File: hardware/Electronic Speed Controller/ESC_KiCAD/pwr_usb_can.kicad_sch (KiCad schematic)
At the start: 31 parts, among them J1 XT60, J3 2x2-2.54MM, J4 S2B-PH-K-S, J5 S2B-PH-K-S, J6 USB TYPE-A, U1 R-78CK5.0-0.5, U2 TLV75533PDBVR, U6 SN65HVD232DR, U8 LM66200DRLR

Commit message: change drivers to C++, add software IIR filtering, improve GCS software
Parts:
- J3: value 2x2-2.54MM -> 2x2-2.54MM
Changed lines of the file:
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@@
 			)
 		)
-		(property "Value" "2x2-2.54MM "
+		(property "Value" "2x2-2.54MM"
 			(at 116.586 135.89 90)
 			(effects

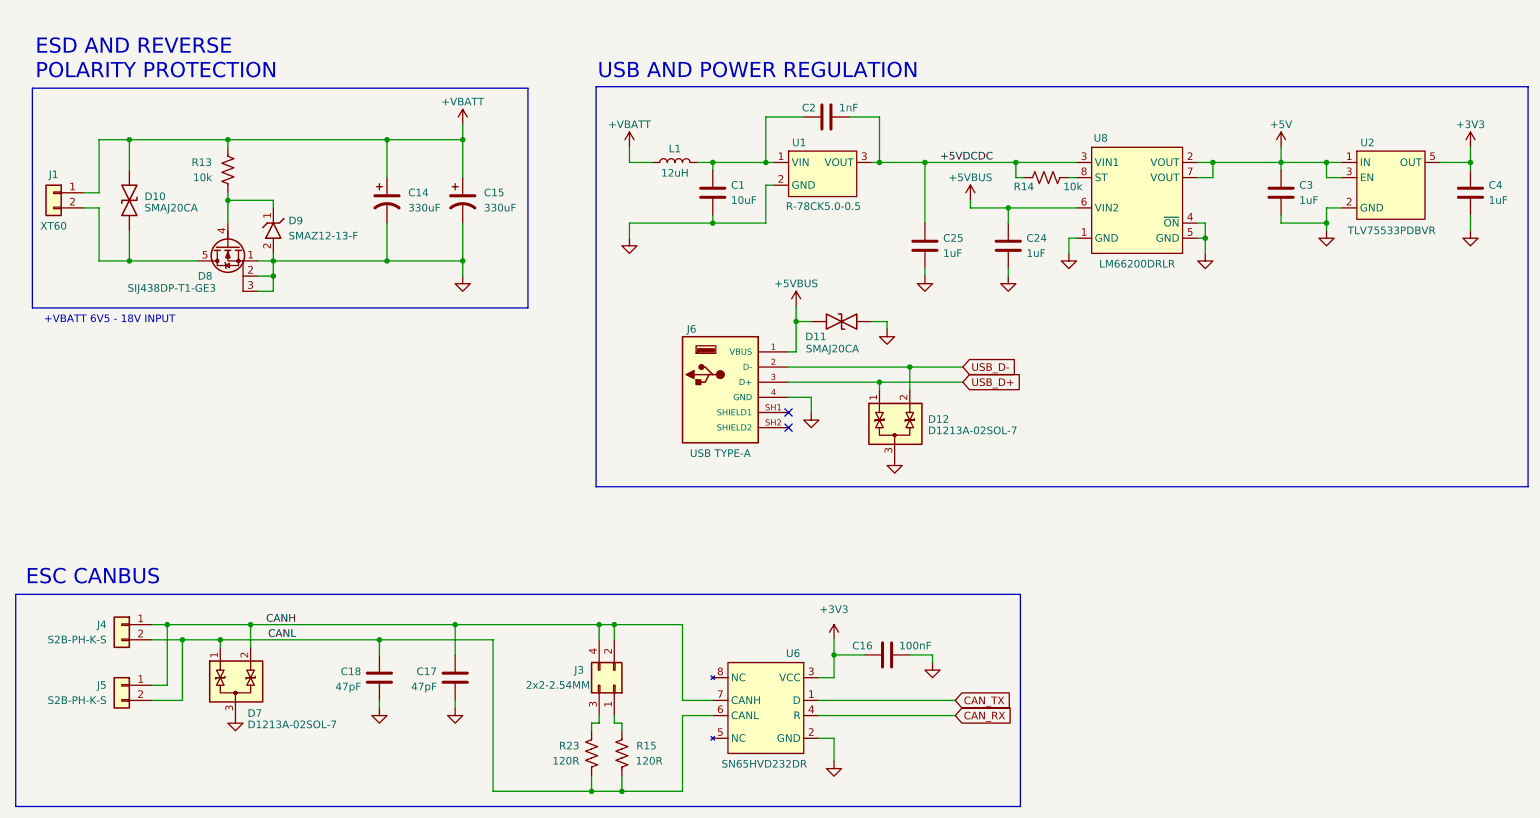
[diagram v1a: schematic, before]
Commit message: finish ESC hardware RevA, CC2500 driver working
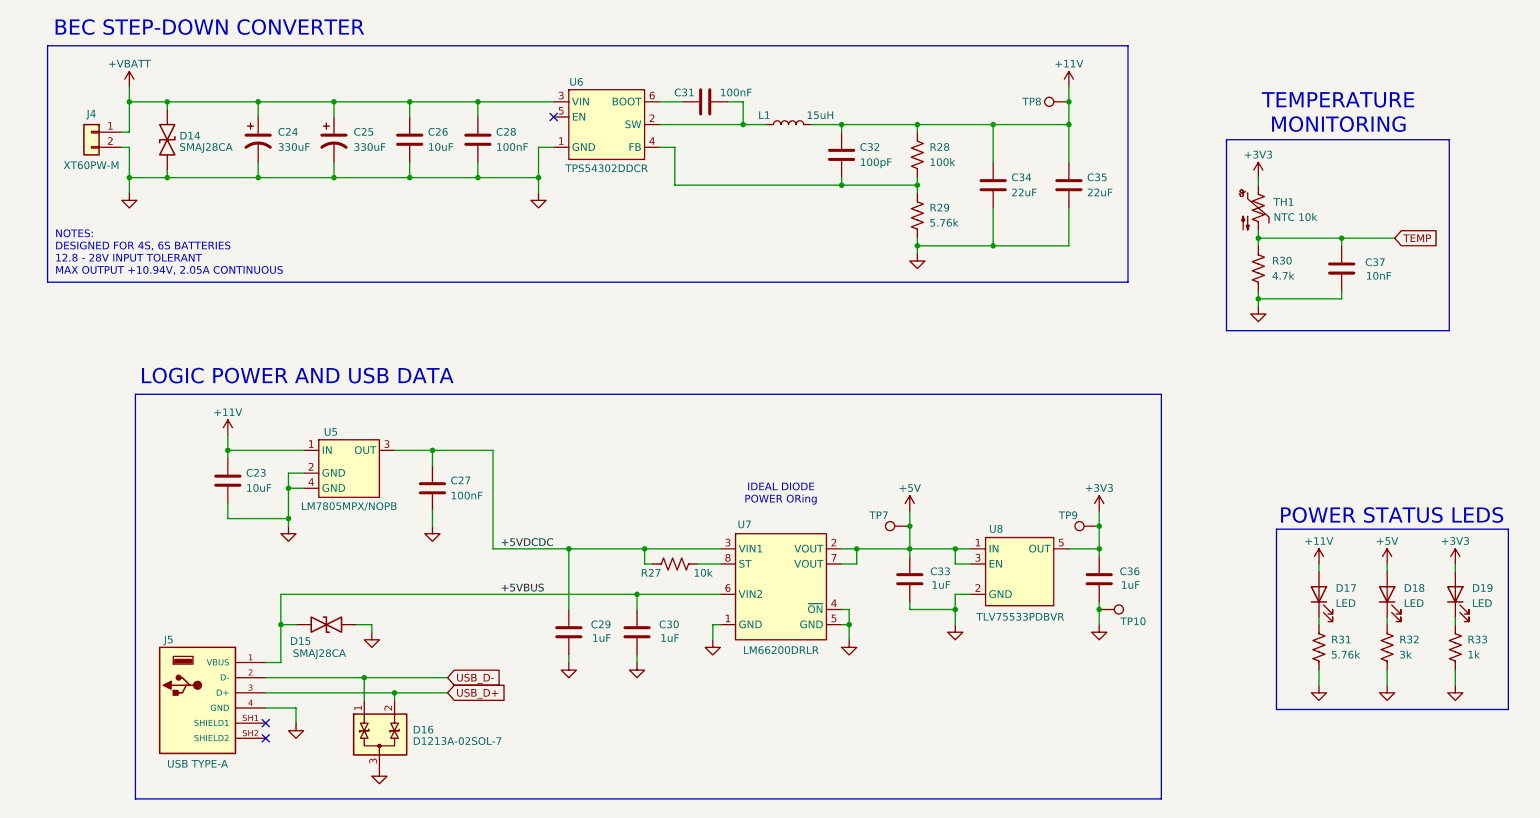
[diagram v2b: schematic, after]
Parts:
- removed C1: 10uF, Capacitors:CAP_1206_3216Metric, symbol Device:C
- removed C14, C15: 330uF, Capacitors:CAP_ALUM_HORIZONTAL, symbol Device:C_Polarized_US
- removed C16: 100nF, Capacitors:CAP_0603_1608Metric, symbol Device:C
- removed C17, C18: 47pF, Capacitors:CAP_0603_1608Metric, symbol Device:C
- removed C2: 1nF, Capacitors:CAP_0603_1608Metric, symbol Device:C
- removed C24, C25, C3, C4: 1uF, Capacitors:CAP_0603_1608Metric, symbol Device:C
- removed D10, D11: SMAJ20CA, Diodes:Littelfuse_SMA, symbol Diodes:TVS_BIDIRECTIONAL
- removed D12, D7: D1213A-02SOL-7, Diodes:DiodesINC_SOT23-3, symbol Diodes:TVS_BIDIRECTIONAL_2CH
- removed D8: SIJ438DP-T1-GE3, Diodes:Vishay_PPAK_SO-8L, symbol Diodes:SiJ438DP
- removed D9: SMAZ12-13-F, Diodes:DiodesINC_SMA, symbol Diodes:ZENER
- removed J1: XT60, Connectors:CONN_MALE_TH_XT60, symbol Connector_Generic:Conn_01x02
- removed J3: 2x2-2.54MM, Connectors:CONN_MALE_TH_2.54MM_2x2, symbol Connector_Generic:Conn_02x02_Odd_Even
- removed J5: S2B-PH-K-S, Connectors:CONN_JST_S2B-PH-K-S, symbol Connector_Generic:Conn_01x02
- removed J6: USB TYPE-A, Connectors:USB2.0_4P_AMPHENOL_87583-2010BLF, symbol Connectors:USB2.0-4P-2SH
- removed R13, R14: 10k, Resistors:RES_0603_1608Metric, symbol Device:R_US
- removed R15, R23: 120R, Resistors:RES_0603_1608Metric, symbol Device:R_US
- removed U1: R-78CK5.0-0.5, ICs:RECOM_SIP-3, symbol ICs:R-78CKxx-0.5
- removed U2: TLV75533PDBVR, ICs:TI_SOT23-5, symbol ICs:TLV755P-DBV
- removed U6: SN65HVD232DR, ICs:TI_SOIC-8, symbol ICs:SN65HVD232D
- removed U8: LM66200DRLR, ICs:TI_SOT-5X3, symbol ICs:LM66200
- added C23, C26: 10uF, Capacitors:CAP_1206_3216Metric, symbol Device:C
- added C24, C25: 330uF, Capacitors:CAP_ALUM_HORIZONTAL, symbol Device:C_Polarized_US
- added C27, C28, C31: 100nF, Capacitors:CAP_0603_1608Metric, symbol Device:C
- added C29, C30, C33, C36: 1uF, Capacitors:CAP_0805_2012Metric, symbol Device:C
- added C32: 100pF, Capacitors:CAP_0603_1608Metric, symbol Device:C
- added C34, C35: 22uF, Capacitors:CAP_0805_2012Metric, symbol Device:C
- added C37: 10nF, Capacitors:CAP_0603_1608Metric, symbol Device:C
- added D14, D15: SMAJ28CA, Diodes:Littelfuse_SMA, symbol Diodes:TVS_BIDIRECTIONAL
- added D16: D1213A-02SOL-7, Diodes:DiodesINC_SOT23-3, symbol Diodes:TVS_BIDIRECTIONAL_2CH
- added D17, D18, D19: LED, Diodes:LED_0603_1608Metric, symbol Device:LED
- added J5: USB TYPE-A, Connectors:USB2.0_4P_AMPHENOL_87583-2010BLF, symbol Connectors:USB2.0-4P-2SH
- added R27: 10k, Resistors:RES_0603_1608Metric, symbol Device:R_US
- added R28: 100k, Resistors:RES_0603_1608Metric, symbol Device:R_US
- added R29, R31: 5.76k, Resistors:RES_0603_1608Metric, symbol Device:R_US
- added R30: 4.7k, Resistors:RES_0603_1608Metric, symbol Device:R_US
- added R32: 3k, Resistors:RES_0603_1608Metric, symbol Device:R_US
- added R33: 1k, Resistors:RES_0603_1608Metric, symbol Device:R_US
- added TH1: NTC 10k, Resistors:RES_0603_1608Metric, symbol Device:Thermistor_NTC_US
- added TP10, TP7, TP8, TP9: TestPoint, TestPoint:TestPoint_Pad_2.0x2.0mm, symbol Connector:TestPoint
- added U5: LM7805MPX/NOPB, ICs:TI_SOT223-4, symbol ICs:LM7805-DCY
- added U6: TPS54302DDCR, ICs:TI_SOT23-6, symbol ICs:TPS54302
- added U7: LM66200DRLR, ICs:TI_SOT-5X3, symbol ICs:LM66200
- added U8: TLV75533PDBVR, ICs:TI_SOT23-5, symbol ICs:TLV755P-DBV
- J4: value S2B-PH-K-S -> XT60PW-M; footprint Connectors:CONN_JST_S2B-PH-K-S -> Connectors:CONN_MALE_TH_XT60PW; JLCPCB Part # C173752 -> C98732; Manufacturer JST Sales America Inc. -> Changzhou Amass Elec; Manufacturer Part # S2B-PH-K-S -> XT60PW-M
- L1: value 12uH -> 15uH; footprint Inductors:Abracon_ASPI-6045S -> Inductors:L_6045S; JLCPCB Part # C187451 -> C83374; Manufacturer Abracon LLC -> Shenzhen Sunlord Electronics Co., Ltd.; Manufacturer Part # ASPI-6045S-120M-T -> SWPA6045S150MT
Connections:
- net CANH is gone; now on net +VBATT: J4.1 (Pin_1)
- net CANL is gone; now on net GND: J4.2 (Pin_2)
- net +3V3: now also C36.2, D19.2 (A), TH1.1, TP9.1, U8.5 (OUT)
- net +5V: now also C33.2, D18.2 (A), TP7.1, U7.2 (VOUT), U7.7 (VOUT), U8.1 (IN), U8.3 (EN)
- net +5VBUS: now also C30.2, D15.1 (K), J5.1 (VBUS), U7.6 (VIN2)
- net +5VDCDC: now also C27.2, C29.2, R27.1, U5.3 (OUT), U7.3 (VIN1)
- net +VBATT: now also C24.1, C25.1, C26.1, C28.2, D14.1 (K), U6.3 (VIN); no longer L1.1
- net GND: now also C23.2, C24.2, C25.2, C26.2, C27.1, C28.1, C29.1, C30.1, C33.1, C34.2, C35.2, C36.1, C37.1, D14.2 (A), D15.2 (A), D16.3 (A), J5.4 (GND), R29.2, R30.2, R31.2, R32.2, R33.2, TP10.1, U5.2 (GND), U5.4 (GND), U6.1 (GND), U7.1 (GND), U7.4 (~{ON}), U7.5 (GND), U8.2 (GND)
- net USB_D+: now also D16.2 (K), J5.3 (D+)
- net USB_D-: now also D16.1 (K), J5.2 (D-)
- net +11V: now reaches L1.2
- net +11V: now also C23.1, C32.1, C34.1, C35.1, D17.2 (A), R28.1, TP8.1, U5.1 (IN)
- new net: C32.2, R28.2, R29.1, U6.4 (FB)
- new net: C31.2, L1.1, U6.2 (SW)
- new net: C31.1, U6.6 (BOOT)
- new net: R27.2, U7.8 (ST)
- new net: D19.1 (K), R33.1
- new net: D17.1 (K), R31.1
- new net: D18.1 (K), R32.1
- new net TEMP: C37.2, R30.1, TH1.2
- no-connect marks 2 -> 3
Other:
- note added: "BEC STEP-DOWN CONVERTER"
- note added: "IDEAL DIODE POWER ORing"
- note added: "LOGIC POWER AND USB DATA"
- note added: "NOTES: DESIGNED FOR 4S, 6S BATTERIES 12.8 - 28V INPUT TOLERANT MAX OUTPUT +10.94V, 2.05A CONTINUOUS"
- note added: "POWER STATUS LEDS"
- note added: "TEMPERATURE MONITORING"
- note removed: "+VBATT 6V5 - 18V INPUT"
- note removed: "ESC CANBUS"
- note removed: "ESD AND REVERSE POLARITY PROTECTION"
- note removed: "USB AND POWER REGULATION"
- title: POWER REGULATION, USB, AND CANBUS -> POWER AND USB DATA
